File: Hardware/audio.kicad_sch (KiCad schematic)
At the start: 35 parts, among them J13 ANT_BNC, J14 ANT_BNC, J15 Audio IN, Q3 MMBT2222A, U10 Si4732, U9 LM358, X1 Q13FC1350000400

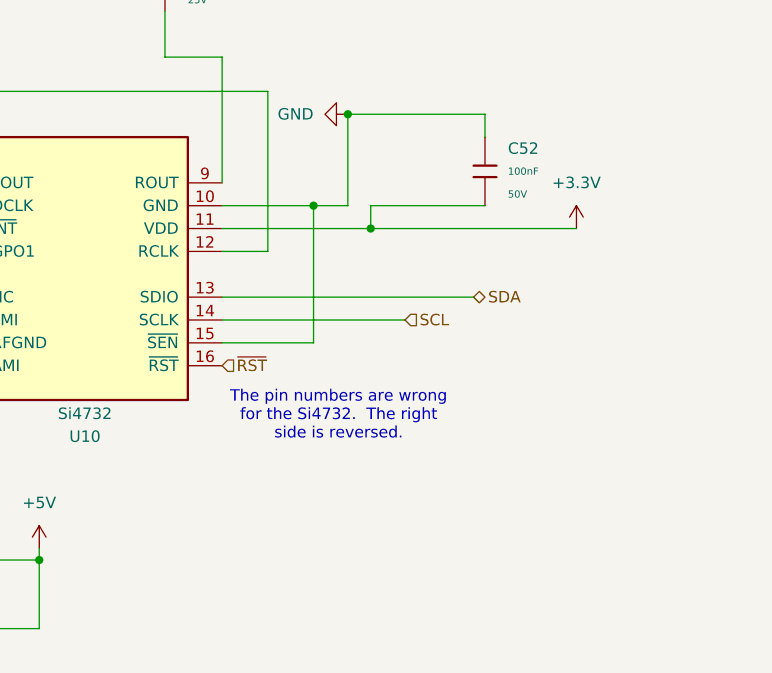
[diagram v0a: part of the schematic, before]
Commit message: Fixed si4732 schematic, added README for Pico
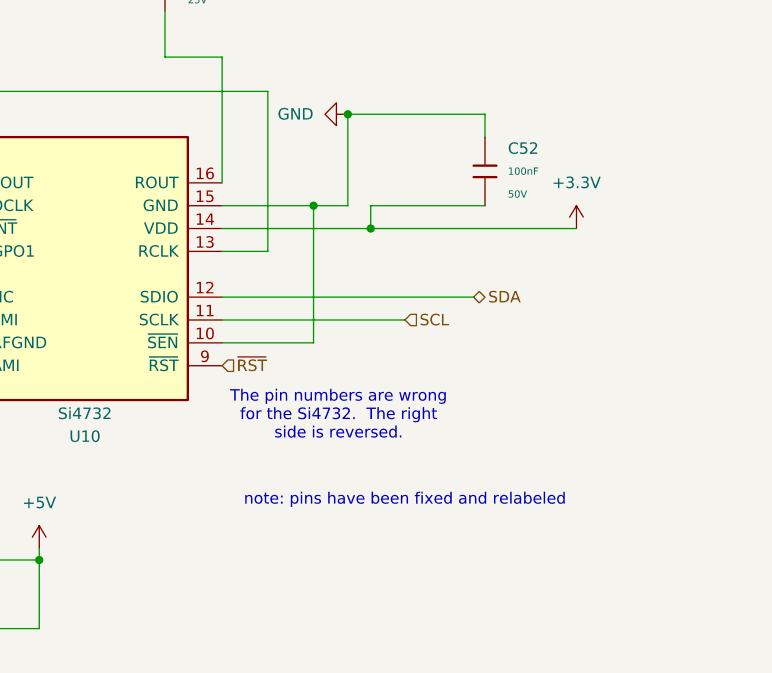
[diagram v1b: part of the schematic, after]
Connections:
- net +3.3V: now also U10.14 (VDD); no longer U10.11 (VDD)
- net SCL: now also U10.11 (SCLK); no longer U10.14 (SCLK)
- net SDA: now also U10.12 (SDIO); no longer U10.13 (SDIO)
- net ~{RST}: now also U10.9 (~{RST}); no longer U10.16 (~{RST})
- net at C36.2, X1.2: now also U10.13 (RCLK); no longer U10.12 (RCLK)
- net at C45.2: now also U10.16 (ROUT); no longer U10.9 (ROUT)
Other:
- note added: "note: pins have been fixed and relabeled"
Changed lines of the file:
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@@
+		)
+	)
+	(text "note: pins have been fixed and relabeled"
+		(exclude_from_sim no)
+		(at 127 143.256 0)
+		(effects
+			(font
+				(size 1.27 1.27)
+			)
 		)
 	)
